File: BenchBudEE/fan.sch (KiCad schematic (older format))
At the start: 8 parts

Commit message: arduino schematic and interconnection
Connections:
- net labels added: CUR_MEAS, FAN_EN, FAN_OUT+, FAN_OUT-, TACH_MEAS
- net labels removed: Current_Measure, FAN_IN, POWER+, POWER-, TACH_OUT
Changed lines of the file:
@@
 Sheet 8 9
 Title ""
-Date "16 feb 2014"
+Date "17 feb 2014"
 Rev ""
 Comp ""
@@
 $EndDescr
 Text HLabel 9950 3300 2    60   Output ~ 0
-POWER+
-Text HLabel 9950 3600 2    60   Input ~ 0
-POWER-
+FAN_OUT+
+Text HLabel 9950 3600 2    60   Output ~ 0
+FAN_OUT-
 Text HLabel 9950 4000 2    60   Input ~ 0
 TACH_IN
-Text HLabel 1450 5300 0    60   Output ~ 0
-TACH_OUT
+Text HLabel 1500 5300 0    60   Output ~ 0
+TACH_MEAS
 Text HLabel 1500 4500 0    60   Input ~ 0
-FAN_IN
+FAN_EN
 $Comp
 L LM324 U?
@@
 Wire Wire Line
 	8600 5300 1450 5300
-Text HLabel 1450 5100 0    60   Output ~ 0
-Current_Measure
+Text HLabel 1500 5100 0    60   Output ~ 0
+CUR_MEAS
 Wire Wire Line
 	1450 5100 7800 5100

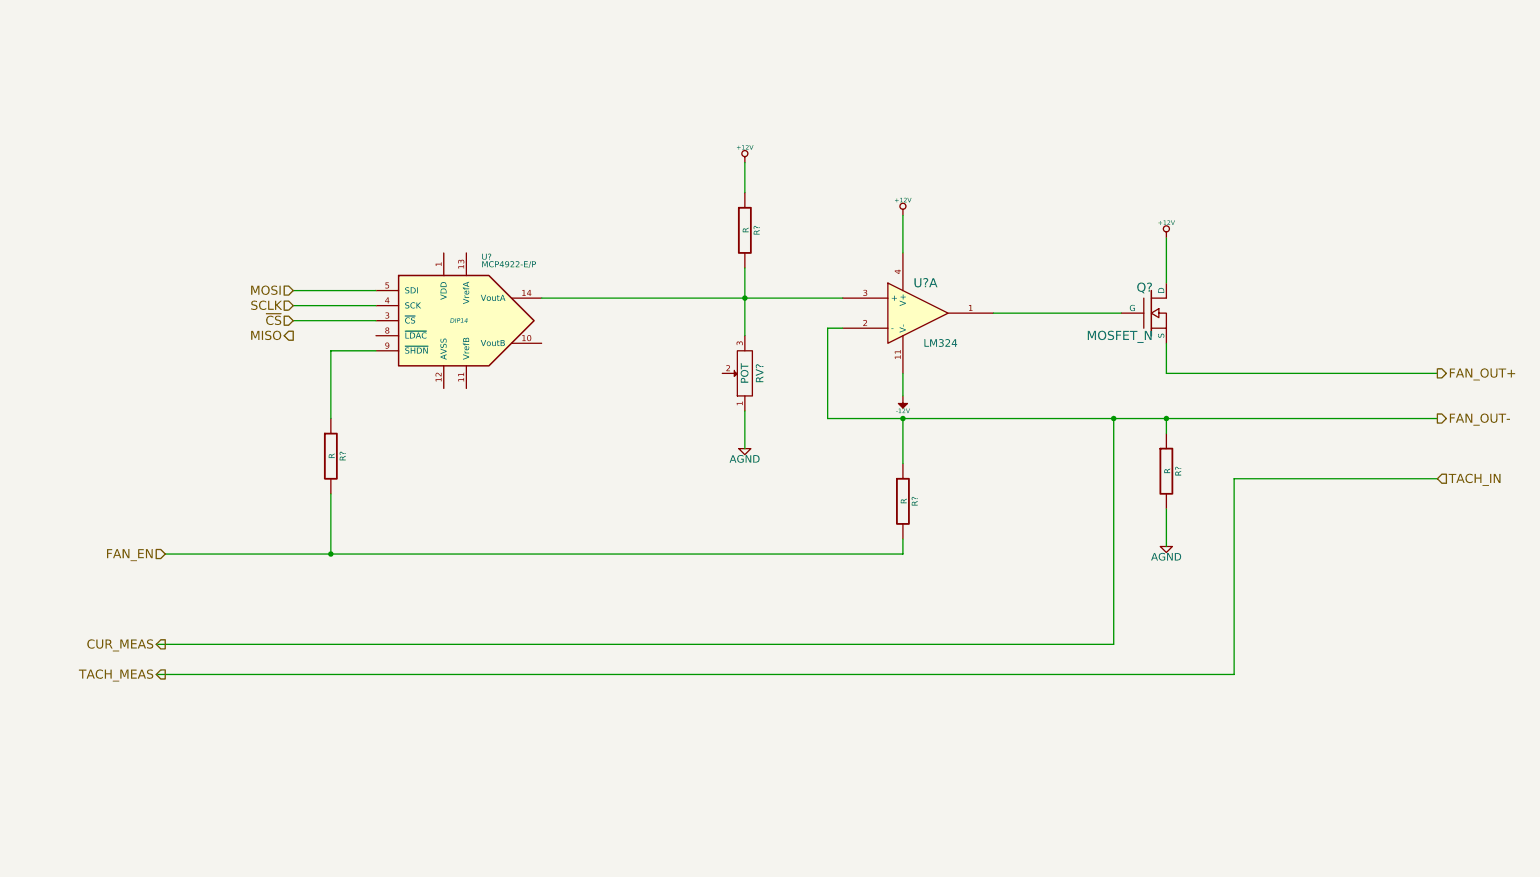
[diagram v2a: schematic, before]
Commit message: fan/current supply refactor
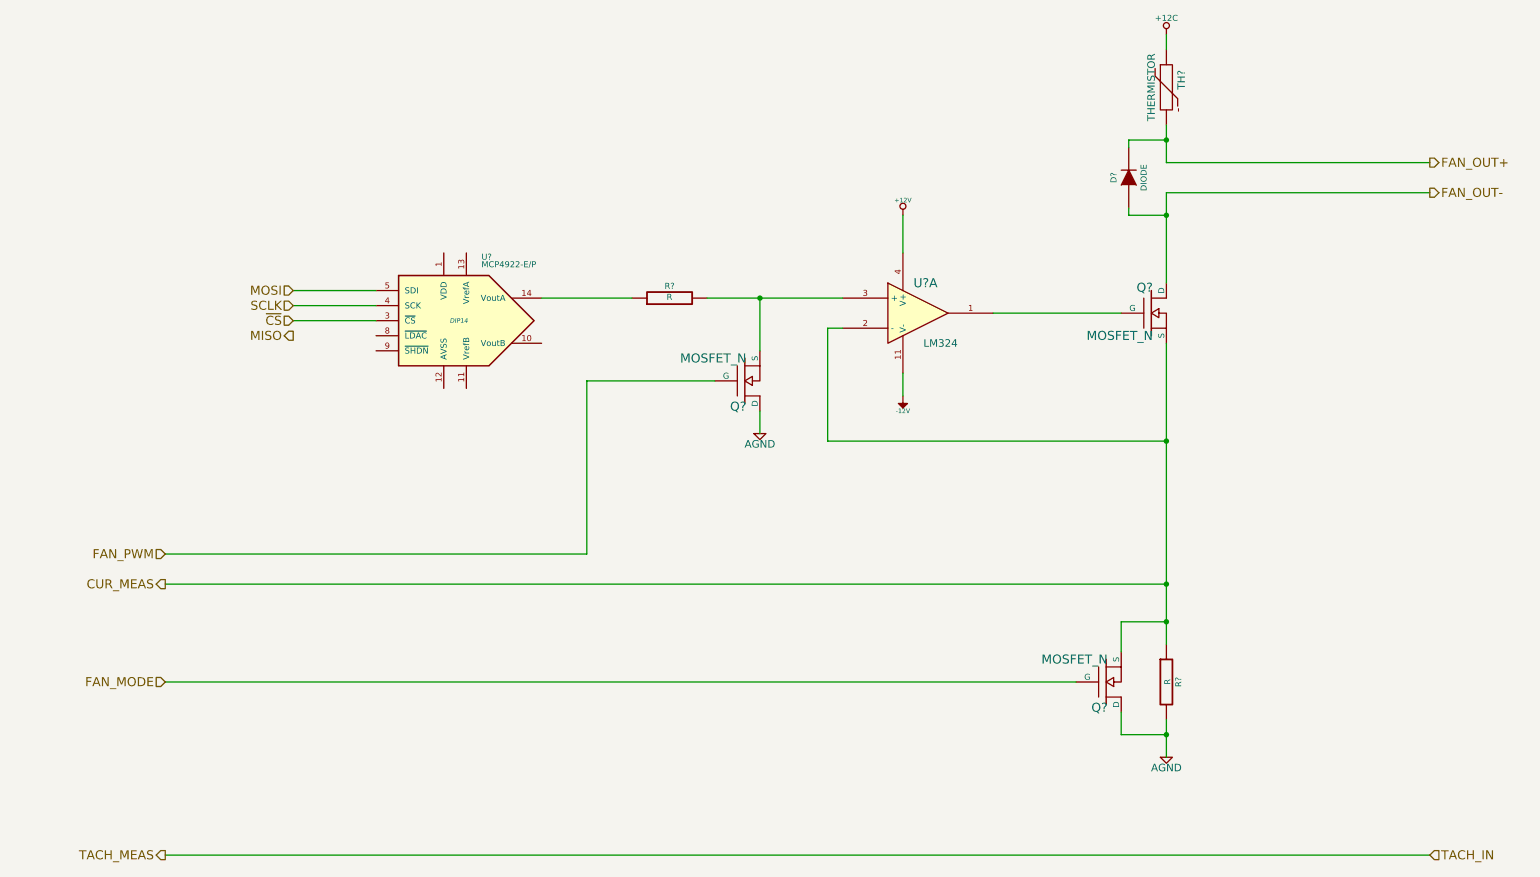
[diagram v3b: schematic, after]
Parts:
- removed R? (x2): R, ~, symbol R
- removed RV?: POT, ~, symbol POT
- added D?: DIODE, ~, symbol DIODE
- added Q? (x2): MOSFET_N, ~, symbol MOSFET_N
- added TH?: THERMISTOR, ~, symbol THERMISTOR
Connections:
- net labels added: +12C, FAN_MODE, FAN_PWM
- net labels removed: FAN_EN
- wire segments 29 -> 34
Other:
- moved on the sheet: R?
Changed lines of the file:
@@
 $Descr A4 11693 8268
 encoding utf-8
-Sheet 8 9
+Sheet 7 9
 Title ""
 Date "17 feb 2014"
@@
 Comment4 ""
 $EndDescr
-Text HLabel 9950 3300 2    60   Output ~ 0
+Text HLabel 9900 1900 2    60   Output ~ 0
 FAN_OUT+
-Text HLabel 9950 3600 2    60   Output ~ 0
+Text HLabel 9900 2100 2    60   Output ~ 0
 FAN_OUT-
-Text HLabel 9950 4000 2    60   Input ~ 0
+Text HLabel 9900 6500 2    60   Input ~ 0
 TACH_IN
-Text HLabel 1500 5300 0    60   Output ~ 0
+Text HLabel 1500 6500 0    60   Output ~ 0
 TACH_MEAS
 Text HLabel 1500 4500 0    60   Input ~ 0
-FAN_EN
+FAN_PWM
 $Comp
 L LM324 U?
@@
 $EndComp
 $Comp
-L +12V #PWR?
-U 1 1 52F69E76
-P 8150 2400
-F 0 "#PWR?" H 8150 2350 20  0001 C CNN
-F 1 "+12V" H 8150 2500 30  0000 C CNN
-F 2 "" H 8150 2400 60  0000 C CNN
-F 3 "" H 8150 2400 60  0000 C CNN
-	1    8150 2400
-	1    0    0    -1
-$EndComp
-Wire Wire Line
-	9950 3300 8150 3300
-Wire Wire Line
-	8150 3300 8150 3100
-Wire Wire Line
-	7850 2900 7000 2900
-$Comp
 L R R?
 U 1 1 52F69E89
-P 8150 3950
-F 0 "R?" V 8230 3950 40  0000 C CNN
-F 1 "R" V 8157 3951 40  0000 C CNN
-F 2 "~" V 8080 3950 30  0000 C CNN
-F 3 "~" H 8150 3950 30  0000 C CNN
-	1    8150 3950
-	1    0    0    -1
-$EndComp
-Wire Wire Line
-	8150 3600 8150 3700
-Wire Wire Line
-	5900 3600 9950 3600
+P 8150 5350
+F 0 "R?" V 8230 5350 40  0000 C CNN
+F 1 "R" V 8157 5351 40  0000 C CNN
+F 2 "~" V 8080 5350 30  0000 C CNN
+F 3 "~" H 8150 5350 30  0000 C CNN
+	1    8150 5350
+	1    0    0    -1
+$EndComp
 $Comp
 L AGND #PWR?
 U 1 1 52F69E9C
-P 8150 4450
-F 0 "#PWR?" H 8150 4450 40  0001 C CNN
-F 1 "AGND" H 8150 4380 50  0000 C CNN
-F 2 "" H 8150 4450 60  0000 C CNN
-F 3 "" H 8150 4450 60  0000 C CNN
-	1    8150 4450
-	1    0    0    -1
-$EndComp
-Wire Wire Line
-	8150 4450 8150 4200
-Wire Wire Line
-	5900 3600 5900 3000
-Wire Wire Line
-	5900 3000 6000 3000
-Connection ~ 8150 3600
-Wire Wire Line
-	8150 2400 8150 2700
+P 8150 5850
+F 0 "#PWR?" H 8150 5850 40  0001 C CNN
+F 1 "AGND" H 8150 5780 50  0000 C CNN
+F 2 "" H 8150 5850 60  0000 C CNN
+F 3 "" H 8150 5850 60  0000 C CNN
+	1    8150 5850
+	1    0    0    -1
+$EndComp
 $Comp
 L +12V #PWR?
@@
 	1    0    0    -1
 $EndComp
-Wire Wire Line
-	6400 2250 6400 2500
 $Comp
 L -12V #PWR?
@@
 	-1   0    0    1
 $EndComp
-Wire Wire Line
-	6400 3450 6400 3300
 $Comp
 L R R?
 U 1 1 52F69F17
-P 5350 2350
-F 0 "R?" V 5430 2350 40  0000 C CNN
-F 1 "R" V 5357 2351 40  0000 C CNN
-F 2 "~" V 5280 2350 30  0000 C CNN
-F 3 "~" H 5350 2350 30  0000 C CNN
-	1    5350 2350
-	1    0    0    -1
-$EndComp
-$Comp
-L +12V #PWR?
-U 1 1 52F69F1D
-P 5350 1900
-F 0 "#PWR?" H 5350 1850 20  0001 C CNN
-F 1 "+12V" H 5350 2000 30  0000 C CNN
-F 2 "" H 5350 1900 60  0000 C CNN
-F 3 "" H 5350 1900 60  0000 C CNN
-	1    5350 1900
-	1    0    0    -1
-$EndComp
-Wire Wire Line
-	5350 1900 5350 2100
-Wire Wire Line
-	5350 2600 5350 3050
-Wire Wire Line
-	4000 2800 6000 2800
-$Comp
-L POT RV?
-U 1 1 52F69F40
-P 5350 3300
-F 0 "RV?" H 5350 3200 50  0000 C CNN
-F 1 "POT" H 5350 3300 50  0000 C CNN
-F 2 "~" H 5350 3300 60  0000 C CNN
-F 3 "~" H 5350 3300 60  0000 C CNN
-	1    5350 3300
+P 4850 2800
+F 0 "R?" V 4930 2800 40  0000 C CNN
+F 1 "R" V 4857 2801 40  0000 C CNN
+F 2 "~" V 4780 2800 30  0000 C CNN
+F 3 "~" H 4850 2800 30  0000 C CNN
+	1    4850 2800
 	0    -1   -1   0
 $EndComp
-$Comp
-L AGND #PWR?
-U 1 1 52F69F4D
-P 5350 3800
-F 0 "#PWR?" H 5350 3800 40  0001 C CNN
-F 1 "AGND" H 5350 3730 50  0000 C CNN
-F 2 "" H 5350 3800 60  0000 C CNN
-F 3 "" H 5350 3800 60  0000 C CNN
-	1    5350 3800
-	1    0    0    -1
-$EndComp
-Wire Wire Line
-	5350 3800 5350 3550
-Connection ~ 5350 2800
 $Comp
 L MCP4922-E/P U?
@@
 	1    0    0    -1
 $EndComp
-Wire Wire Line
-	9950 4000 8600 4000
-Wire Wire Line
-	8600 4000 8600 5300
-Wire Wire Line
-	8600 5300 1450 5300
-Text HLabel 1500 5100 0    60   Output ~ 0
+Text HLabel 1500 4700 0    60   Output ~ 0
 CUR_MEAS
-Wire Wire Line
-	1450 5100 7800 5100
-Wire Wire Line
-	7800 5100 7800 3600
-Connection ~ 7800 3600
-$Comp
-L R R?
-U 1 1 52F69FB4
-P 6400 4150
-F 0 "R?" V 6480 4150 40  0000 C CNN
-F 1 "R" V 6407 4151 40  0000 C CNN
-F 2 "~" V 6330 4150 30  0000 C CNN
-F 3 "~" H 6400 4150 30  0000 C CNN
-	1    6400 4150
-	1    0    0    -1
-$EndComp
-Wire Wire Line
-	6400 3900 6400 3600
-Connection ~ 6400 3600
-Wire Wire Line
-	6400 4500 6400 4400
-Wire Wire Line
-	1500 4500 6400 4500
 Text HLabel 2350 2750 0    60   Input ~ 0
 MOSI
@@
 Text HLabel 2350 2850 0    60   Input ~ 0
 SCLK
+$Comp
+L MOSFET_N Q?
+U 1 1 5302A08A
+P 7750 5350
+F 0 "Q?" H 7760 5520 60  0000 R CNN
+F 1 "MOSFET_N" H 7760 5200 60  0000 R CNN
+F 2 "~" H 7750 5350 60  0000 C CNN
+F 3 "~" H 7750 5350 60  0000 C CNN
+	1    7750 5350
+	1    0    0    1
+$EndComp
+$Comp
+L THERMISTOR TH?
+U 1 1 5302A0A1
+P 8150 1400
+F 0 "TH?" V 8250 1450 50  0000 C CNN
+F 1 "THERMISTOR" V 8050 1400 50  0000 C CNN
+F 2 "~" H 8150 1400 60  0000 C CNN
+F 3 "~" H 8150 1400 60  0000 C CNN
+	1    8150 1400
+	1    0    0    -1
+$EndComp
+$Comp
+L DIODE D?
+U 1 1 5302A12D
+P 7900 2000
+F 0 "D?" H 7900 2100 40  0000 C CNN
+F 1 "DIODE" H 7900 1900 40  0000 C CNN
+F 2 "~" H 7900 2000 60  0000 C CNN
+F 3 "~" H 7900 2000 60  0000 C CNN
+	1    7900 2000
+	0    -1   -1   0
+$EndComp
+Wire Wire Line
+	8150 3100 8150 5100
+Wire Wire Line
+	7850 2900 7000 2900
+Wire Wire Line
+	8150 5850 8150 5600
+Wire Wire Line
+	5900 3000 5900 3750
+Wire Wire Line
+	5900 3000 6000 3000
+Wire Wire Line
+	6400 2250 6400 2500
+Wire Wire Line
+	6400 3450 6400 3300
 Wire Wire Line
 	2350 2750 2900 2750
@@
 Wire Wire Line
 	2350 2950 2900 2950
-$Comp
-L R R?
-U 1 1 52F6A0B1
-P 2600 3850
-F 0 "R?" V 2680 3850 40  0000 C CNN
-F 1 "R" V 2607 3851 40  0000 C CNN
-F 2 "~" V 2530 3850 30  0000 C CNN
-F 3 "~" H 2600 3850 30  0000 C CNN
-	1    2600 3850
-	1    0    0    -1
-$EndComp
-Wire Wire Line
-	2600 4100 2600 4500
-Connection ~ 2600 4500
-Wire Wire Line
-	2600 3600 2600 3150
-Wire Wire Line
-	2600 3150 2900 3150
+Wire Wire Line
+	8150 1150 8150 1050
+Wire Wire Line
+	8150 1650 8150 1900
+Wire Wire Line
+	8150 1900 9900 1900
+Wire Wire Line
+	9900 2100 8150 2100
+Wire Wire Line
+	8150 2100 8150 2700
+Wire Wire Line
+	7900 1800 7900 1750
+Wire Wire Line
+	7900 1750 8150 1750
+Connection ~ 8150 1750
+Wire Wire Line
+	7900 2200 7900 2250
+Wire Wire Line
+	7900 2250 8150 2250
+Connection ~ 8150 2250
+Wire Wire Line
+	7850 5150 7850 4950
+Wire Wire Line
+	7850 4950 8150 4950
+Connection ~ 8150 4950
+Wire Wire Line
+	7850 5550 7850 5700
+Wire Wire Line
+	7850 5700 8150 5700
+Connection ~ 8150 5700
+Wire Wire Line
+	9900 6500 1500 6500
+Wire Wire Line
+	5900 3750 8150 3750
+Connection ~ 8150 3750
+Wire Wire Line
+	1500 4500 4300 4500
+Wire Wire Line
+	1500 4700 8150 4700
+Connection ~ 8150 4700
+$Comp
+L MOSFET_N Q?
+U 1 1 5302A36F
+P 5350 3350
+F 0 "Q?" H 5360 3520 60  0000 R CNN
+F 1 "MOSFET_N" H 5360 3200 60  0000 R CNN
+F 2 "~" H 5350 3350 60  0000 C CNN
+F 3 "~" H 5350 3350 60  0000 C CNN
+	1    5350 3350
+	1    0    0    1
+$EndComp
+Wire Wire Line
+	5150 3350 4300 3350
+Wire Wire Line
+	4300 3350 4300 4500
+Wire Wire Line
+	5450 3150 5450 2800
+Connection ~ 5450 2800
+Wire Wire Line
+	4600 2800 4000 2800
+Wire Wire Line
+	5100 2800 6000 2800
+$Comp
+L AGND #PWR?
+U 1 1 5302A42A
+P 5450 3700
+F 0 "#PWR?" H 5450 3700 40  0001 C CNN
+F 1 "AGND" H 5450 3630 50  0000 C CNN
+F 2 "" H 5450 3700 60  0000 C CNN
+F 3 "" H 5450 3700 60  0000 C CNN
+	1    5450 3700
+	1    0    0    -1
+$EndComp
+Wire Wire Line
+	5450 3700 5450 3550
+Wire Wire Line
+	7550 5350 1500 5350
+Text HLabel 1500 5350 0    60   Input ~ 0
+FAN_MODE
+$Comp
+L +12C #PWR?
+U 1 1 5302A7FF
+P 8150 1050
+F 0 "#PWR?" H 8150 1020 30  0001 C CNN
+F 1 "+12C" H 8150 1160 40  0000 C CNN
+F 2 "" H 8150 1050 60  0000 C CNN
+F 3 "" H 8150 1050 60  0000 C CNN
+	1    8150 1050
+	1    0    0    -1
+$EndComp
 $EndSCHEMATC
